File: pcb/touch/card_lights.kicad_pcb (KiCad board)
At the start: 2 copper layers, 22 x 44 mm, 12 parts, among them J1 TOUCH PAD, J2 LED_PAD, J3 LED_PAD, J4 LED_PAD, U1 ATtiny10-TS, U2 TTP223E-HA6

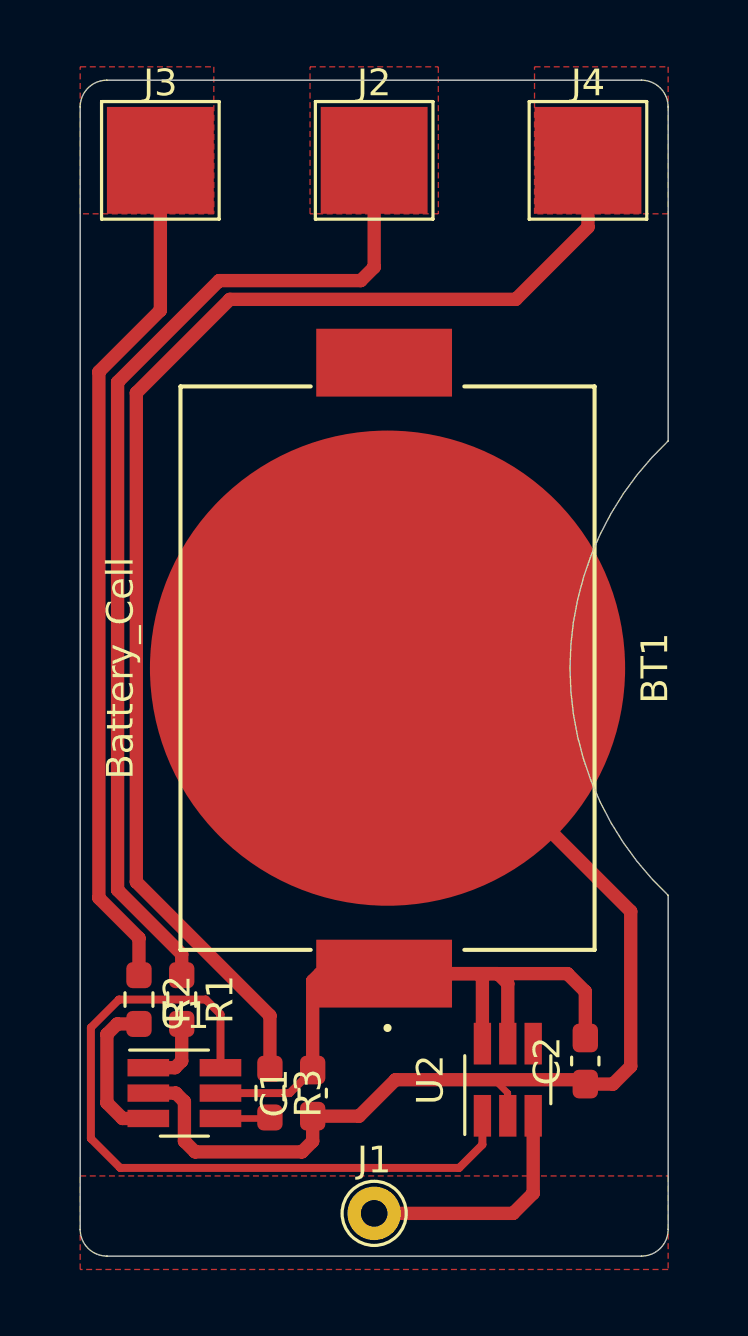
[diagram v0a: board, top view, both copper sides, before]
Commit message: add new components, start making pretty for PCB manufacture
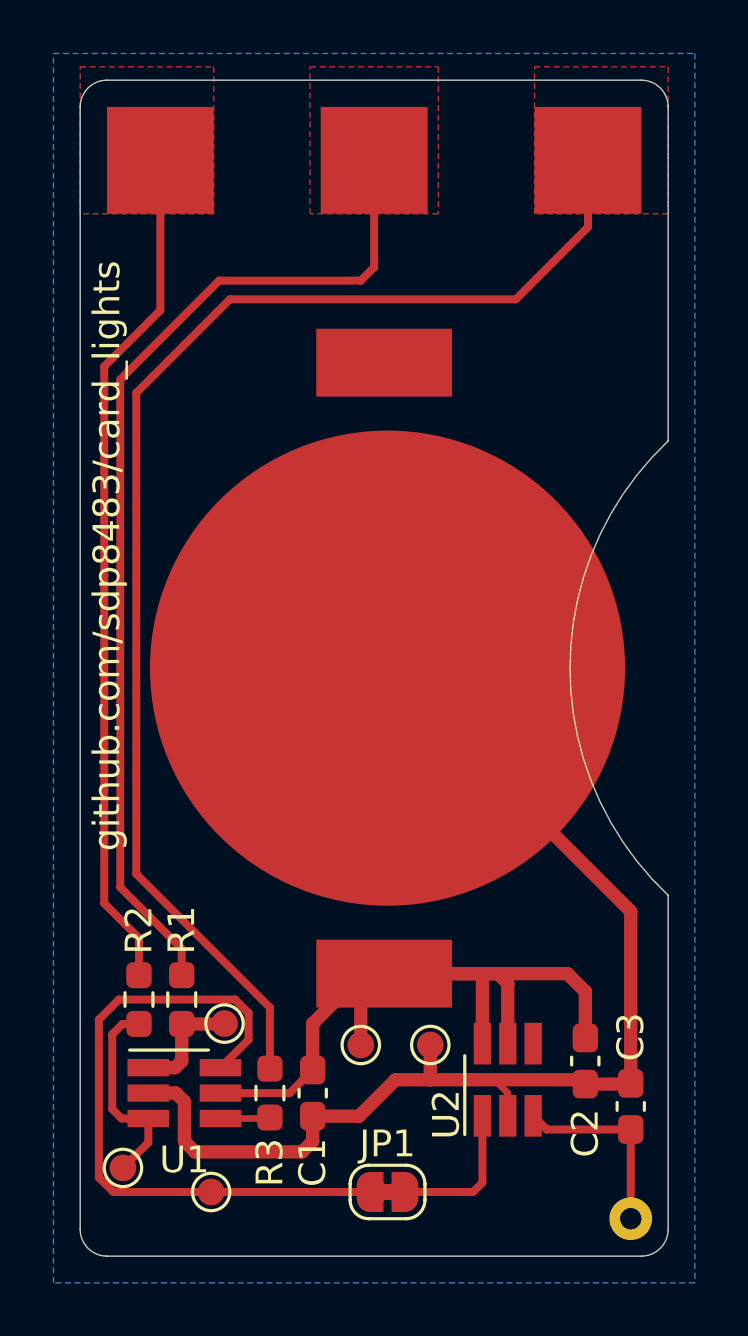
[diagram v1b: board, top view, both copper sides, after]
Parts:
- added C3: 10p, Capacitor_SMD:C_0603_1608Metric_Pad1.08x0.95mm_HandSolder, F.Cu at (120.6, 138.4)
- added JP1: PROG, Jumper:SolderJumper-2_P1.3mm_Bridged_RoundedPad1.0x1.5mm, F.Cu at (111.5, 141.6)
- added TP1: TestPoint, TestPoint:TestPoint_Pad_D1.0mm, F.Cu at (110.5, 136.1)
- added TP2: TestPoint, TestPoint:TestPoint_Pad_D1.0mm, F.Cu at (105.4, 135.3)
- added TP3: TestPoint, TestPoint:TestPoint_Pad_D1.0mm, F.Cu at (101.6, 140.7)
- added TP4: TestPoint, TestPoint:TestPoint_Pad_D1.0mm, F.Cu at (104.9, 141.6)
- added TP5: TestPoint, TestPoint:TestPoint_Pad_D1.0mm, F.Cu at (113.1, 136.1)
- moved J1 9.60 mm to (120.6, 142.6)
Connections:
- U2 pad 1: /PB3 -> Net-(JP1-Pad2)
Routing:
- net Net-(JP1-Pad2): track 0.00 -> 5.54 mm
- net /PB3: track 28.2 -> 24.9 mm
- net +3V0: track 29.1 -> 31.2 mm
- net /PB1: track 5.72 -> 7.70 mm
- net /TOUCH: track 9.16 -> 7.20 mm
- net GND: track 45.8 -> 47.5 mm
- net /PB0: track 2.74 -> 4.35 mm
- added copper zone on B.Cu, net /TOUCH
- removed copper zone on F.Cu, net /TOUCH
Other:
- board text added: "github.com/sdp8483/card_lights"

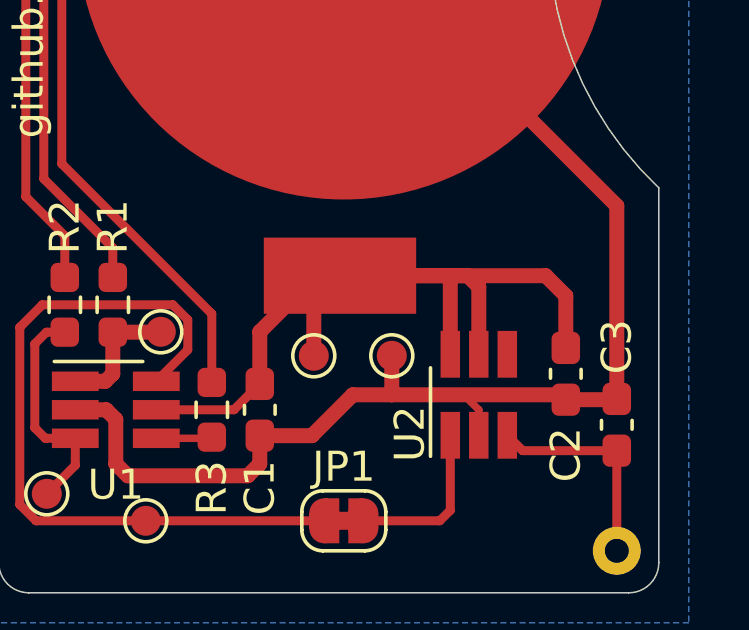
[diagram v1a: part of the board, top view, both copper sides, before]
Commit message: update touch controller to not use output toggle
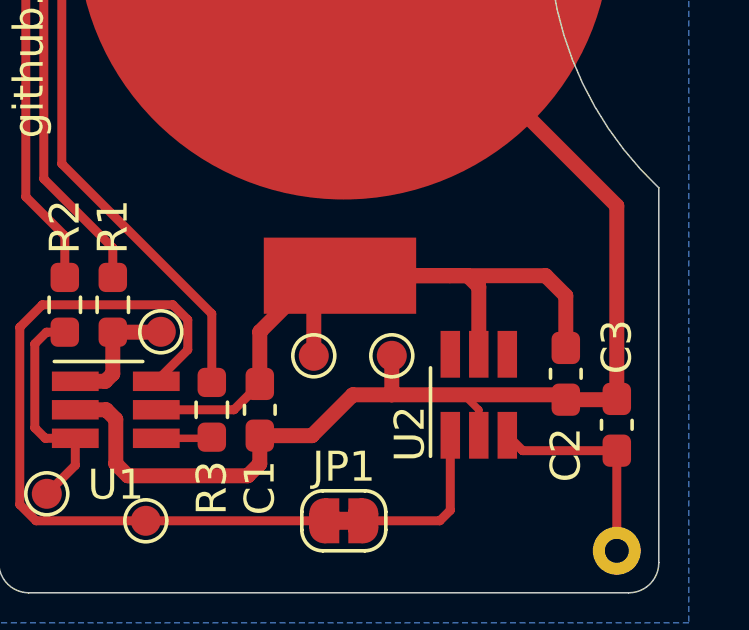
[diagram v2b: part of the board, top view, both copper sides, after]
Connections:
- U2 pad 6: +3V0 -> Net-(U2-Pad6)
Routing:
- net +3V0: track 31.2 -> 28.6 mm

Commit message: pcb layout changes
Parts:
- removed J1: TOUCH PAD, TestPoint:TestPoint_THTPad_D2.0mm_Drill1.0mm
- added G***: LOGO, PL_logo:logo_height_4mm, F.Cu at (118.5, 111.5)
- added JP2: Jumper_NC_Small, Jumper:SolderJumper-2_P1.3mm_Bridged_RoundedPad1.0x1.5mm, F.Cu at (118.4, 139.8)
- added JP3: Jumper_NC_Small, Jumper:SolderJumper-2_P1.3mm_Open_RoundedPad1.0x1.5mm, F.Cu at (115.0, 141.4)
- added JP4: Jumper_NC_Small, Jumper:SolderJumper-2_P1.3mm_Bridged_RoundedPad1.0x1.5mm, F.Cu at (118.4, 142.4)
- added TP6: TestPoint, TestPoint:TestPoint_Pad_3.0x3.0mm, F.Cu at (111.5, 142.0)
- JP1: value PROG -> Jumper_NC_Small
- moved TP5 2.72 mm to (110.5, 136.9)
- moved JP1 2.62 mm to (111.2, 139.0)
- moved TP1 2.57 mm to (108.0, 135.5)
- moved C3 2.06 mm to (119.3, 136.8)
- moved C2 1.40 mm to (117.5, 136.8)
- moved U2 1.22 mm to (114.8, 137.6)
- moved TP4 0.86 mm to (105.6, 141.1)
- moved TP3 0.50 mm to (101.6, 140.2)
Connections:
- C3 pad 1: /TOUCH -> Net-(C3-Pad1)
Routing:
- net GND: track 47.5 -> 39.5 mm
- net +3V0: track 28.6 -> 21.1 mm
- net Net-(JP1-Pad2): track 5.54 -> 2.02 mm
- net Net-(JP3-Pad2): track 0.00 -> 3.10 mm
- net Net-(C3-Pad1): track 0.00 -> 2.24 mm
- net Net-(J1-Pad1): track 0.00 -> 1.61 mm, vias 0 -> 1
- added copper zone on B.Cu, net Net-(J1-Pad1)
- removed copper zone on B.Cu, net /TOUCH
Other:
- board text added: "PB0"
- board text added: "PB1"
- board text added: "PB2"
- board text added: "Touch"
- board text added: "V1.0"
